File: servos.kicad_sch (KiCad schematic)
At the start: 17 parts, among them J10 Conn_01x03_Male, J18 Conn_01x03_Male, J19 Conn_01x03_Male, J5 Conn_01x03_Male, J6 Conn_01x03_Male, J7 Conn_01x03_Male, J8 Conn_01x03_Male, J9 Conn_01x03_Male, Q6 DMN2011UTS

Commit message: add power status LEDs
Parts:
- removed D28: LED_Small, LED_SMD:LED_0805_2012Metric, symbol Device:LED_Small
- removed R4: 220R, Resistor_SMD:R_0603_1608Metric, symbol Device:R_Small
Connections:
- net GND: no longer D29.1 (K)
- net GND_SERVO_2: now also D29.1 (K)
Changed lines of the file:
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@@
-	(wire
-		(pts
-			(xy 151.13 72.39) (xy 156.21 72.39)
-		)
-		(stroke
-			(width 0)
-			(type default)
-		)
-	)
 	(wire
 		(pts
@@
 	(wire
 		(pts
-			(xy 129.54 72.39) (xy 135.89 72.39)
-		)
-		(stroke
-			(width 0)
-			(type default)
-		)
-	)
-	(wire
-		(pts
 			(xy 210.82 109.22) (xy 210.82 124.46)
 		)
@@
 		(pts
 			(xy 99.06 171.45) (xy 101.6 171.45)
-		)
-		(stroke
-			(width 0)
-			(type default)
-		)
-	)
-	(wire
-		(pts
-			(xy 140.97 72.39) (xy 146.05 72.39)
 		)
 		(stroke
@@
 			)
 			(justify left bottom)
+		)
+	)
+	(label "GND_SERVO_2"
+		(at 130.81 81.28 180)
+		(fields_autoplaced yes)
+		(effects
+			(font
+				(size 1.27 1.27)
+			)
+			(justify right bottom)
 		)
 	)
@@
 		)
 	)
-	(global_label "GND"
-		(shape input)
-		(at 129.54 72.39 180)
-		(fields_autoplaced yes)
-		(effects
-			(font
-				(size 1.27 1.27)
-			)
-			(justify right)
-		)
-		(property "Intersheetrefs" "${INTERSHEET_REFS}"
-			(at 123.2564 72.3106 0)
-			(effects
-				(font
-					(size 1.27 1.27)
-				)
-				(justify right)
-				(hide yes)
-			)
-		)
-	)
 	(global_label "ENABLE_SERVO_POWER_1"
 		(shape input)
@@
 		)
 	)
-	(global_label "GND"
-		(shape input)
-		(at 129.54 81.28 180)
-		(fields_autoplaced yes)
-		(effects
-			(font
-				(size 1.27 1.27)
-			)
-			(justify right)
-		)
-		(property "Intersheetrefs" "${INTERSHEET_REFS}"
-			(at 123.2564 81.2006 0)
-			(effects
-				(font
-					(size 1.27 1.27)
-				)
-				(justify right)
-				(hide yes)
-			)
-		)
-	)
 	(global_label "SERVO_2"
 		(shape input)
@@
 		(shape input)
 		(at 231.14 45.72 0)
-		(fields_autoplaced yes)
-		(effects
-			(font
-				(size 1.27 1.27)
-			)
-			(justify left)
-		)
-	)
-	(hierarchical_label "SERVO_POWER_1"
-		(shape input)
-		(at 156.21 72.39 0)
 		(fields_autoplaced yes)
 		(effects
@@
 	(symbol
 		(lib_id "Device:LED_Small")
-		(at 138.43 72.39 0)
-		(unit 1)
-		(exclude_from_sim no)
-		(in_bom yes)
-		(on_board yes)
-		(dnp no)
-		(fields_autoplaced yes)
-		(property "Reference" "D28"
-			(at 138.4935 66.04 0)
-			(effects
-				(font
-					(size 1.27 1.27)
-				)
-			)
-		)
-		(property "Value" "LED_Small"
-			(at 138.4935 68.58 0)
-			(effects
-				(font
-					(size 1.27 1.27)
-				)
-			)
-		)
-		(property "Footprint" "LED_SMD:LED_0805_2012Metric"
-			(at 138.43 72.39 90)
-			(effects
-				(font
-					(size 1.27 1.27)
-				)
-				(hide yes)
-			)
-		)
-		(property "Datasheet" "~"
-			(at 138.43 72.39 90)
-			(effects
-				(font
-					(size 1.27 1.27)
-				)
-				(hide yes)
-			)
-		)
-		(property "Description" ""
-			(at 138.43 72.39 0)
-			(effects
-				(font
-					(size 1.27 1.27)
-				)
-				(hide yes)
-			)
-		)
-		(pin "1"
-		)
-		(pin "2"
-		)
-		(instances
-			(project ""
-				(path "/e63e39d7-6ac0-4ffd-8aa3-1841a4541b55/0c74f7ab-c5ff-45ed-b8c2-3c7ab63bdd9d"
-					(reference "D28")
-					(unit 1)
-				)
-			)
-		)
-	)
-	(symbol
-		(lib_id "Device:LED_Small")
 		(at 138.43 81.28 0)
 		(unit 1)
@@
 					(unit 1)
 				)
-			)
-		)
-	)
-	(symbol
-		(lib_id "Device:R_Small")
-		(at 148.59 72.39 90)
-		(unit 1)
-		(exclude_from_sim no)
-		(in_bom yes)
-		(on_board yes)
-		(dnp no)
-		(fields_autoplaced yes)
-		(property "Reference" "R4"
-			(at 148.59 66.04 90)
-			(effects
-				(font
-					(size 1.27 1.27)
-				)
-			)
-		)
-		(property "Value" "220R"
-			(at 148.59 68.58 90)
-			(effects
-				(font
-					(size 1.27 1.27)
-				)
-			)
-		)
-		(property "Footprint" "Resistor_SMD:R_0603_1608Metric"
-			(at 148.59 72.39 0)
-			(effects
-				(font
-					(size 1.27 1.27)
-				)
-				(hide yes)
-			)
-		)
-		(property "Datasheet" "~"
-			(at 148.59 72.39 0)
-			(effects
-				(font
-					(size 1.27 1.27)
-				)
-				(hide yes)
-			)
-		)
-		(property "Description" ""
-			(at 148.59 72.39 0)
-			(effects
-				(font
-					(size 1.27 1.27)
-				)
-				(hide yes)
-			)
-		)
-		(pin "1"
-		)
-		(pin "2"
-		)
-		(instances
-			(project ""
-				(path "/e63e39d7-6ac0-4ffd-8aa3-1841a4541b55/0c74f7ab-c5ff-45ed-b8c2-3c7ab63bdd9d"
-					(reference "R4")
-					(unit 1)
-				)

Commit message: fix warnings + add internal layers + add Uart to steppers (TX only
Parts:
- J10, J18, J19, J5, J6, J7, J8, J9: symbol Connector:Conn_01x03_Male -> Connector:Conn_01x03_Pin
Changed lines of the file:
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@@
 			)
 		)
-		(property "Description" ""
+		(property "Description" "Diode"
 			(at 116.84 176.53 0)
 			(effects
@@
 			)
 		)
+		(property "Sim.Device" "D"
+			(at 116.84 176.53 0)
+			(effects
+				(font
+					(size 1.27 1.27)
+				)
+				(hide yes)
+			)
+		)
+		(property "Sim.Pins" "1=K 2=A"
+			(at 116.84 176.53 0)
+			(effects
+				(font
+					(size 1.27 1.27)
+				)
+				(hide yes)
+			)
+		)
 		(pin "1"
 		)
@@
 	)
 	(symbol
-		(lib_id "Connector:Conn_01x03_Male")
+		(lib_id "Connector:Conn_01x03_Pin")
 		(at 210.82 74.93 270)
 		(unit 1)
@@
 			)
 		)
-		(property "Description" ""
+		(property "Description" "Generic connector, single row, 01x03, script generated"
 			(at 210.82 74.93 0)
 			(effects
@@
 	)
 	(symbol
-		(lib_id "Connector:Conn_01x03_Male")
+		(lib_id "Connector:Conn_01x03_Pin")
 		(at 210.82 104.14 270)
 		(unit 1)
@@
 			)
 		)
-		(property "Description" ""
+		(property "Description" "Generic connector, single row, 01x03, script generated"
 			(at 210.82 104.14 0)
 			(effects
@@
 	)
 	(symbol
-		(lib_id "Connector:Conn_01x03_Male")
+		(lib_id "Connector:Conn_01x03_Pin")
 		(at 210.82 52.07 270)
 		(unit 1)
@@
 			)
 		)
-		(property "Description" ""
+		(property "Description" "Generic connector, single row, 01x03, script generated"
 			(at 210.82 52.07 0)
 			(effects
@@
 			)
 		)
-		(property "Description" ""
+		(property "Description" "Diode"
 			(at 215.9 152.4 0)
 			(effects
@@
 			)
 		)
+		(property "Sim.Device" "D"
+			(at 215.9 152.4 0)
+			(effects
+				(font
+					(size 1.27 1.27)
+				)
+				(hide yes)
+			)
+		)
+		(property "Sim.Pins" "1=K 2=A"
+			(at 215.9 152.4 0)
+			(effects
+				(font
+					(size 1.27 1.27)
+				)
+				(hide yes)
+			)
+		)
 		(pin "1"
 		)
@@
 	)
 	(symbol
-		(lib_id "Connector:Conn_01x03_Male")
+		(lib_id "Connector:Conn_01x03_Pin")
 		(at 210.82 63.5 270)
 		(unit 1)
@@
 			)
 		)
-		(property "Description" ""
+		(property "Description" "Generic connector, single row, 01x03, script generated"
 			(at 210.82 63.5 0)
 			(effects
@@
 			)
 		)
-		(property "Description" ""
+		(property "Description" "Diode"
+			(at 220.98 52.07 0)
+			(effects
+				(font
+					(size 1.27 1.27)
+				)
+				(hide yes)
+			)
+		)
+		(property "Sim.Device" "D"
+			(at 220.98 52.07 0)
+			(effects
+				(font
+					(size 1.27 1.27)
+				)
+				(hide yes)
+			)
+		)
+		(property "Sim.Pins" "1=K 2=A"
 			(at 220.98 52.07 0)
 			(effects
@@
 	)
 	(symbol
-		(lib_id "Connector:Conn_01x03_Male")
+		(lib_id "Connector:Conn_01x03_Pin")
 		(at 210.82 142.24 270)
 		(unit 1)
@@
 			)
 		)
-		(property "Description" ""
+		(property "Description" "Generic connector, single row, 01x03, script generated"
 			(at 210.82 142.24 0)
 			(effects
@@
 	)
 	(symbol
-		(lib_id "Connector:Conn_01x03_Male")
+		(lib_id "Connector:Conn_01x03_Pin")
 		(at 210.82 88.9 270)
 		(unit 1)
@@
 			)
 		)
-		(property "Description" ""
+		(property "Description" "Generic connector, single row, 01x03, script generated"
 			(at 210.82 88.9 0)
 			(effects
@@
 	)
 	(symbol
-		(lib_id "Connector:Conn_01x03_Male")
+		(lib_id "Connector:Conn_01x03_Pin")
 		(at 210.82 130.81 270)
 		(unit 1)
@@
 			)
 		)
-		(property "Description" ""
+		(property "Description" "Generic connector, single row, 01x03, script generated"
 			(at 210.82 130.81 0)
 			(effects
@@
 	)
 	(symbol
-		(lib_id "Connector:Conn_01x03_Male")
+		(lib_id "Connector:Conn_01x03_Pin")
 		(at 210.82 119.38 270)
 		(unit 1)
@@
 			)
 		)
-		(property "Description" ""
+		(property "Description" "Generic connector, single row, 01x03, script generated"
 			(at 210.82 119.38 0)
 			(effects

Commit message: add capa for servos
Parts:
- added C33: 470µF, Capacitor_THT:CP_Radial_D7.5mm_P2.50mm, symbol Device:C_Polarized
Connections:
- net GND_SERVO_2: now also C33.2
- net SERVO_POWER_1: now also C33.1
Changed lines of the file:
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@@
+	)
+	(junction
+		(at 229.87 57.15)
+		(diameter 0)
+		(color 0 0 0 0)
+	)
+	(junction
+		(at 229.87 45.72)
+		(diameter 0)
+		(color 0 0 0 0)
 	)
 	(junction
@@
 	(wire
 		(pts
+			(xy 229.87 55.88) (xy 229.87 57.15)
+		)
+		(stroke
+			(width 0)
+			(type default)
+		)
+	)
+	(wire
+		(pts
 			(xy 93.98 171.45) (xy 96.52 171.45)
 		)
@@
 	(wire
 		(pts
+			(xy 229.87 45.72) (xy 229.87 48.26)
+		)
+		(stroke
+			(width 0)
+			(type default)
+		)
+	)
+	(wire
+		(pts
 			(xy 210.82 135.89) (xy 210.82 147.32)
 		)
@@
 	(wire
 		(pts
-			(xy 220.98 45.72) (xy 231.14 45.72)
+			(xy 220.98 45.72) (xy 229.87 45.72)
 		)
 		(stroke
@@
 	(wire
 		(pts
-			(xy 220.98 57.15) (xy 233.68 57.15)
+			(xy 229.87 57.15) (xy 233.68 57.15)
+		)
+		(stroke
+			(width 0)
+			(type default)
+		)
+	)
+	(wire
+		(pts
+			(xy 220.98 57.15) (xy 229.87 57.15)
 		)
 		(stroke
@@
 		(pts
 			(xy 213.36 57.15) (xy 220.98 57.15)
+		)
+		(stroke
+			(width 0)
+			(type default)
+		)
+	)
+	(wire
+		(pts
+			(xy 229.87 45.72) (xy 231.14 45.72)
 		)
 		(stroke
@@
 					(unit 1)
 				)
+			)
+		)
+	)
+	(symbol
+		(lib_id "Device:C_Polarized")
+		(at 229.87 52.07 0)
+		(unit 1)
+		(exclude_from_sim no)
+		(in_bom yes)
+		(on_board yes)
+		(dnp no)
+		(fields_autoplaced yes)
+		(property "Reference" "C33"
+			(at 233.68 49.9109 0)
+			(effects
+				(font
+					(size 1.27 1.27)
+				)
+				(justify left)
+			)
+		)
+		(property "Value" "470µF"
+			(at 233.68 52.4509 0)
+			(effects
+				(font
+					(size 1.27 1.27)
+				)
+				(justify left)
+			)
+		)
+		(property "Footprint" "Capacitor_THT:CP_Radial_D7.5mm_P2.50mm"
+			(at 230.8352 55.88 0)
+			(effects
+				(font
+					(size 1.27 1.27)
+				)
+				(hide yes)
+			)
+		)
+		(property "Datasheet" "~"
+			(at 229.87 52.07 0)
+			(effects
+				(font
+					(size 1.27 1.27)
+				)
+				(hide yes)
+			)
+		)
+		(property "Description" "Polarized capacitor"
+			(at 229.87 52.07 0)
+			(effects
+				(font
+					(size 1.27 1.27)
+				)
+				(hide yes)
+			)
+		)
+		(pin "2"
+		)
+		(pin "1"
+		)
+		(instances
+			(project ""
+				(path "/e63e39d7-6ac0-4ffd-8aa3-1841a4541b55/0c74f7ab-c5ff-45ed-b8c2-3c7ab63bdd9d"
+					(reference "C33")
+					(unit 1)
+				)

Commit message: Add BOM
Add LCSC reference and correct few footprint acording bom
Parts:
- C33: LCSC# (none) -> C106619
- D29: value LED_Small -> LED_R; LCSC# (none) -> C965812
- D34, D35, D5: value D -> D_Zener_Small; footprint Diode_SMD:D_1206_3216Metric -> Diode_SMD:D_SOD-123; LCSC# (none) -> C908230
- J10, J18, J19, J5, J6, J7, J8, J9: LCSC# (none) -> C2937625
- Q6: LCSC# (none) -> C5245271
- R2: LCSC# (none) -> C2907127
- R5: value 220R -> 5.11kR; LCSC# (none) -> C2933233
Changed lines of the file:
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@@
 	(label "GND_SERVO_2"
 		(at 120.65 171.45 0)
-		(fields_autoplaced yes)
 		(effects
 			(font
@@
 	(label "GND_SERVO_2"
 		(at 233.68 57.15 0)
-		(fields_autoplaced yes)
 		(effects
 			(font
@@
 	(label "GND_SERVO_2"
 		(at 130.81 81.28 180)
-		(fields_autoplaced yes)
 		(effects
 			(font
@@
 	(label "GND_SERVO_2"
 		(at 227.33 148.59 0)
-		(fields_autoplaced yes)
 		(effects
 			(font
@@
 		(shape input)
 		(at 231.14 45.72 0)
-		(fields_autoplaced yes)
 		(effects
 			(font
@@
 		(shape input)
 		(at 229.87 156.21 0)
-		(fields_autoplaced yes)
 		(effects
 			(font
@@
 		(shape input)
 		(at 156.21 81.28 0)
-		(fields_autoplaced yes)
 		(effects
 			(font
@@
 		(shape input)
 		(at 93.98 185.42 0)
-		(fields_autoplaced yes)
 		(effects
 			(font
@@
 			)
 		)
-		(property "Value" "D"
+		(property "Value" "D_Zener_Small"
 			(at 119.38 177.7999 90)
 			(effects
@@
 			)
 		)
-		(property "Footprint" "Diode_SMD:D_1206_3216Metric"
+		(property "Footprint" "Diode_SMD:D_SOD-123"
 			(at 116.84 176.53 0)
 			(effects
@@
 			)
 		)
-		(property "Sim.Device" "D"
-			(at 116.84 176.53 0)
-			(effects
-				(font
-					(size 1.27 1.27)
-				)
-				(hide yes)
-			)
-		)
-		(property "Sim.Pins" "1=K 2=A"
+		(property "LCSC#" "C908230"
 			(at 116.84 176.53 0)
 			(effects
@@
 			)
 		)
+		(property "LCSC#" "C2937625"
+			(at 210.82 74.93 0)
+			(effects
+				(font
+					(size 1.27 1.27)
+				)
+				(hide yes)
+			)
+		)
 		(pin "1"
 		)
@@
 			)
 		)
+		(property "LCSC#" "C2937625"
+			(at 210.82 104.14 0)
+			(effects
+				(font
+					(size 1.27 1.27)
+				)
+				(hide yes)
+			)
+		)
 		(pin "1"
 		)
@@
 			)
 		)
-		(property "Value" "LED_Small"
+		(property "Value" "LED_R"
 			(at 138.4935 77.47 0)
 			(effects
@@
 		)
 		(property "Description" ""
+			(at 138.43 81.28 0)
+			(effects
+				(font
+					(size 1.27 1.27)
+				)
+				(hide yes)
+			)
+		)
+		(property "LCSC#" "C965812"
 			(at 138.43 81.28 0)
 			(effects
@@
 			)
 		)
+		(property "LCSC#" "C2937625"
+			(at 210.82 52.07 0)
+			(effects
+				(font
+					(size 1.27 1.27)
+				)
+				(hide yes)
+			)
+		)
 		(pin "1"
 		)
@@
 			)
 		)
+		(property "LCSC#" "C106619"
+			(at 229.87 52.07 0)
+			(effects
+				(font
+					(size 1.27 1.27)
+				)
+				(hide yes)
+			)
+		)
 		(pin "2"
 		)
@@
 			)
 		)
-		(property "Value" "D"
+		(property "Value" "D_Zener_Small"
 			(at 218.44 153.6699 90)
 			(effects
@@
 			)
 		)
-		(property "Footprint" "Diode_SMD:D_1206_3216Metric"
+		(property "Footprint" "Diode_SMD:D_SOD-123"
 			(at 215.9 152.4 0)
 			(effects
@@
 			)
 		)
-		(property "Sim.Device" "D"
-			(at 215.9 152.4 0)
-			(effects
-				(font
-					(size 1.27 1.27)
-				)
-				(hide yes)
-			)
-		)
-		(property "Sim.Pins" "1=K 2=A"
+		(property "LCSC#" "C908230"
 			(at 215.9 152.4 0)
 			(effects
@@
 			)
 		)
+		(property "LCSC#" "C2937625"
+			(at 210.82 63.5 0)
+			(effects
+				(font
+					(size 1.27 1.27)
+				)
+				(hide yes)
+			)
+		)
 		(pin "1"
 		)
@@
 			)
 		)
-		(property "Value" "D"
+		(property "Value" "D_Zener_Small"
 			(at 223.52 53.3399 90)
 			(effects
@@
 			)
 		)
-		(property "Footprint" "Diode_SMD:D_1206_3216Metric"
+		(property "Footprint" "Diode_SMD:D_SOD-123"
 			(at 220.98 52.07 0)
 			(effects
@@
 			)
 		)
-		(property "Sim.Device" "D"
-			(at 220.98 52.07 0)
-			(effects
-				(font
-					(size 1.27 1.27)
-				)
-				(hide yes)
-			)
-		)
-		(property "Sim.Pins" "1=K 2=A"
+		(property "LCSC#" "C908230"
 			(at 220.98 52.07 0)
 			(effects
@@
 			)
 		)
-		(property "Value" "220R"
+		(property "Value" "5.11kR"
 			(at 148.59 77.47 90)
 			(effects
@@
 		)
 		(property "Description" ""
+			(at 148.59 81.28 0)
+			(effects
+				(font
+					(size 1.27 1.27)
+				)
+				(hide yes)
+			)
+		)
+		(property "LCSC#" "C2933233"
 			(at 148.59 81.28 0)
 			(effects
@@
 			)
 		)
+		(property "LCSC#" "C2937625"
+			(at 210.82 142.24 0)
+			(effects
+				(font
+					(size 1.27 1.27)
+				)
+				(hide yes)
+			)
+		)
 		(pin "1"
 		)
@@
 			)
 		)
+		(property "LCSC#" "C2937625"
+			(at 210.82 88.9 0)
+			(effects
+				(font
+					(size 1.27 1.27)
+				)
+				(hide yes)
+			)
+		)
 		(pin "1"
 		)
@@
 			)
 		)
+		(property "LCSC#" "C2937625"
+			(at 210.82 130.81 0)
+			(effects
+				(font
+					(size 1.27 1.27)
+				)
+				(hide yes)
+			)
+		)
 		(pin "1"
 		)
@@
 			)
 		)
+		(property "LCSC#" "C2937625"
+			(at 210.82 119.38 0)
+			(effects
+				(font
+					(size 1.27 1.27)
+				)
+				(hide yes)
+			)
+		)
 		(pin "1"
 		)
@@
 			)
 		)
+		(property "LCSC#" "C5245271"
+			(at 91.44 176.53 0)
+			(effects
+				(font
+					(size 1.27 1.27)
+				)
+				(hide yes)
+			)
+		)
 		(pin "1"
 		)
@@
 			(at 78.74 176.53 0)
 			(effects
+				(font
+					(size 1.27 1.27)
+				)
+				(hide yes)
+			)
+		)
+		(property "LCSC#" "C2907127"
+			(at 78.74 176.53 0)
+			(effects

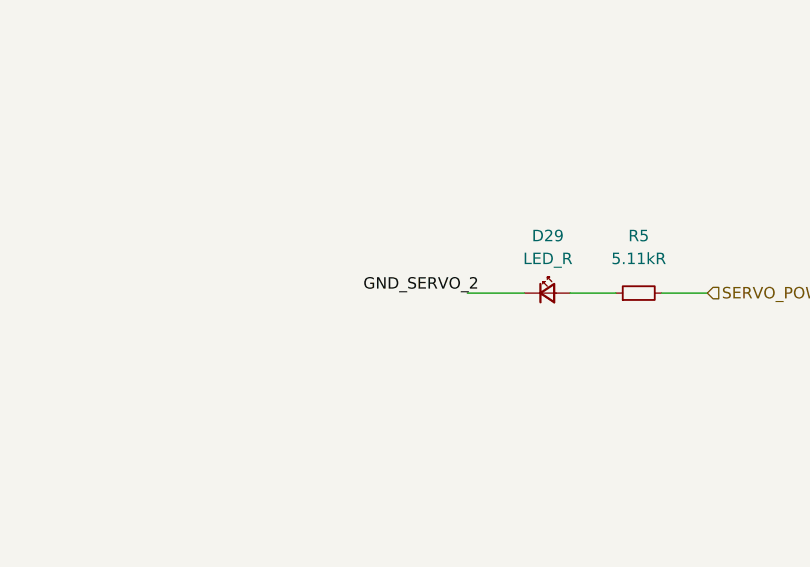
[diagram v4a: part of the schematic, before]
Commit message: update to Kicad 9 + small fixes
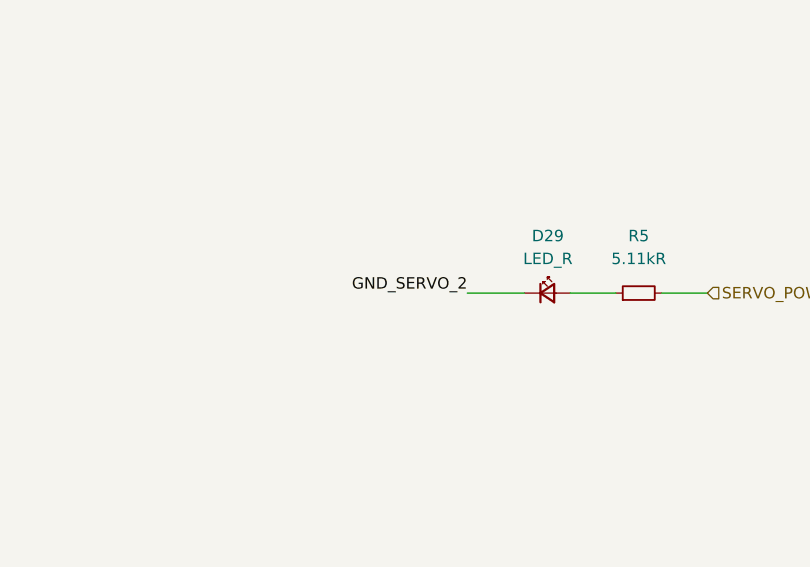
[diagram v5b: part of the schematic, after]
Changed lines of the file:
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@@
 (kicad_sch
-	(version 20231120)
+	(version 20250114)
 	(generator "eeschema")
-	(generator_version "8.0")
+	(generator_version "9.0")
 	(paper "A4")
 	(junction
@@
 	)
 	(label "GND_SERVO_2"
-		(at 130.81 81.28 180)
+		(at 129.54 81.28 180)
 		(effects
 			(font
@@
 		)
 		(property "LCSC#" "C908230"
+			(at 116.84 176.53 0)
+			(effects
+				(font
+					(size 1.27 1.27)
+				)
+				(hide yes)
+			)
+		)
+		(property "Sim.Device" "D"
+			(at 116.84 176.53 0)
+			(effects
+				(font
+					(size 1.27 1.27)
+				)
+				(hide yes)
+			)
+		)
+		(property "Sim.Pins" "1=K 2=A"
 			(at 116.84 176.53 0)
 			(effects
@@
 			)
 		)
-		(property "Description" ""
+		(property "Description" "Light emitting diode, small symbol"
 			(at 138.43 81.28 0)
 			(effects
@@
 		)
 		(property "LCSC#" "C965812"
+			(at 138.43 81.28 0)
+			(effects
+				(font
+					(size 1.27 1.27)
+				)
+				(hide yes)
+			)
+		)
+		(property "Sim.Pin" "1=K 2=A"
 			(at 138.43 81.28 0)
 			(effects
@@
 			)
 		)
+		(property "Sim.Device" "D"
+			(at 215.9 152.4 0)
+			(effects
+				(font
+					(size 1.27 1.27)
+				)
+				(hide yes)
+			)
+		)
+		(property "Sim.Pins" "1=K 2=A"
+			(at 215.9 152.4 0)
+			(effects
+				(font
+					(size 1.27 1.27)
+				)
+				(hide yes)
+			)
+		)
 		(pin "1"
 		)
@@
 			)
 		)
+		(property "Sim.Device" "D"
+			(at 220.98 52.07 0)
+			(effects
+				(font
+					(size 1.27 1.27)
+				)
+				(hide yes)
+			)
+		)
+		(property "Sim.Pins" "1=K 2=A"
+			(at 220.98 52.07 0)
+			(effects
+				(font
+					(size 1.27 1.27)
+				)
+				(hide yes)
+			)
+		)
 		(pin "1"
 		)
@@
 			)
 		)
-		(property "Description" ""
+		(property "Description" "Resistor, small symbol"
 			(at 148.59 81.28 0)
 			(effects
@@
 			)
 		)
-		(property "Description" ""
+		(property "Description" "N-MOSFET transistor 20A, TSSOP-8"
 			(at 91.44 176.53 0)
 			(effects
@@
 			)
 		)
-		(property "Description" ""
+		(property "Description" "Resistor"
 			(at 78.74 176.53 0)
 			(effects
